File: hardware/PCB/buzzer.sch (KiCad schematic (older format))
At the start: 4 parts

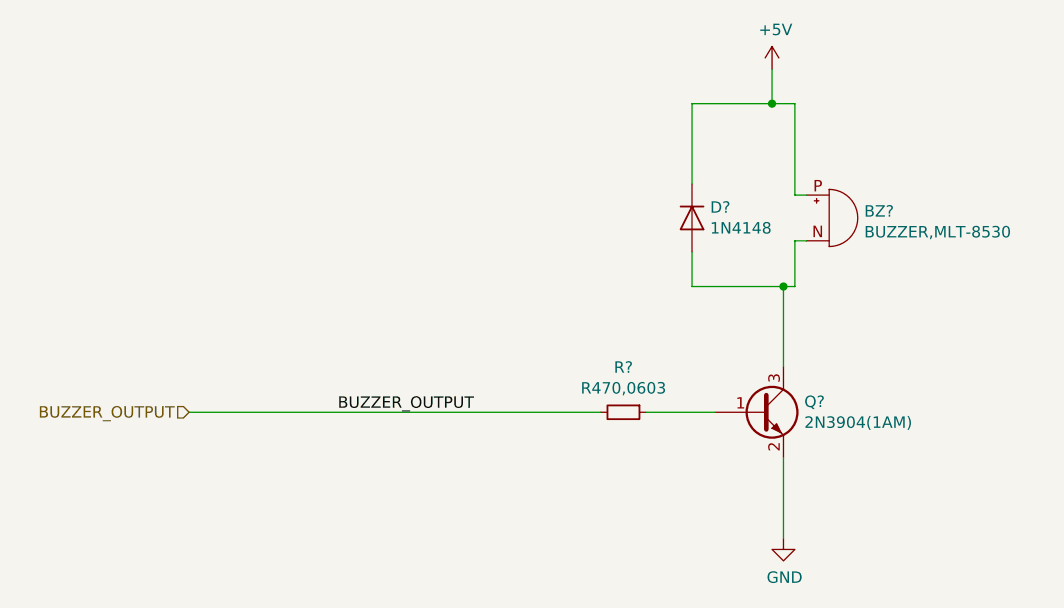
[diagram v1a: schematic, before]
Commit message: sch: update buzzer connection,
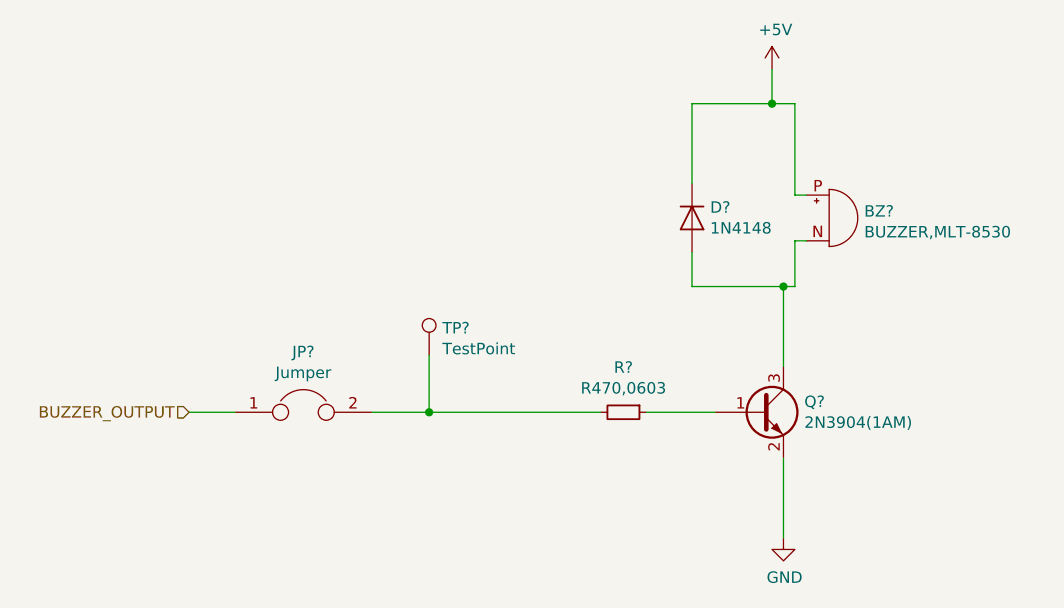
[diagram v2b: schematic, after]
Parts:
- added JP?: Jumper, symbol Device:Jumper
- added TP?: TestPoint, symbol Connector:TestPoint
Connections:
- net BUZZER_OUTPUT: now also JP?.1; no longer R?.2
- new net: JP?.2, R?.2, TP?.1
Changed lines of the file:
@@
 $Descr A4 11693 8268
 encoding utf-8
-Sheet 4 6
+Sheet 1 6
 Title ""
 Date ""
@@
 AR Path="/5E87CEF1/5E91DA5A" Ref="BZ?"  Part="1"
 AR Path="/5E91CDD8/5E91DA5A" Ref="BZ?"  Part="1"
+AR Path="/5E91DA5A" Ref="BZ?"  Part="1"
 F 0 "BZ?" H 8603 2279 50  0000 L CNN
 F 1 "BUZZER,MLT-8530" H 8603 2188 50  0000 L CNN
@@
 AR Path="/5E87CEF1/5E91DA60" Ref="D?"  Part="1"
 AR Path="/5E91CDD8/5E91DA60" Ref="D?"  Part="1"
+AR Path="/5E91DA60" Ref="D?"  Part="1"
 F 0 "D?" V 7804 2329 50  0000 L CNN
 F 1 "1N4148" V 7895 2329 50  0000 L CNN
@@
 AR Path="/5E87CEF1/5E91DA66" Ref="Q?"  Part="1"
 AR Path="/5E91CDD8/5E91DA66" Ref="Q?"  Part="1"
+AR Path="/5E91DA66" Ref="Q?"  Part="1"
 F 0 "Q?" H 8341 3146 50  0000 L CNN
 F 1 "2N3904(1AM)" H 8341 3055 50  0000 L CNN
@@
 AR Path="/5E87CEF1/5E91DA6C" Ref="R?"  Part="1"
 AR Path="/5E91CDD8/5E91DA6C" Ref="R?"  Part="1"
+AR Path="/5E91DA6C" Ref="R?"  Part="1"
 F 0 "R?" V 7354 3100 50  0000 C CNN
 F 1 "R470,0603" V 7445 3100 50  0000 C CNN
@@
 Wire Wire Line
 	8250 3650 8250 3300
-Text Label 6300 3100 0    50   ~ 0
-BUZZER_OUTPUT
-Wire Wire Line
-	5650 3100 7450 3100
 Text HLabel 5650 3100 0    50   Input ~ 0
 BUZZER_OUTPUT
+$Comp
+L Device:Jumper JP?
+U 1 1 5E99CD71
+P 6150 3100
+F 0 "JP?" H 6150 3364 50  0000 C CNN
+F 1 "Jumper" H 6150 3273 50  0000 C CNN
+F 2 "" H 6150 3100 50  0001 C CNN
+F 3 "~" H 6150 3100 50  0001 C CNN
+	1    6150 3100
+	1    0    0    -1
+$EndComp
+Wire Wire Line
+	5850 3100 5650 3100
+Wire Wire Line
+	7450 3100 6700 3100
+$Comp
+L Connector:TestPoint TP?
+U 1 1 5E99F415
+P 6700 2850
+F 0 "TP?" H 6758 2968 50  0000 L CNN
+F 1 "TestPoint" H 6758 2877 50  0000 L CNN
+F 2 "" H 6900 2850 50  0001 C CNN
+F 3 "~" H 6900 2850 50  0001 C CNN
+	1    6700 2850
+	1    0    0    -1
+$EndComp
+Wire Wire Line
+	6700 2850 6700 3100
+Connection ~ 6700 3100
+Wire Wire Line
+	6700 3100 6450 3100
 $EndSCHEMATC

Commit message: update rtl8723 circuit,
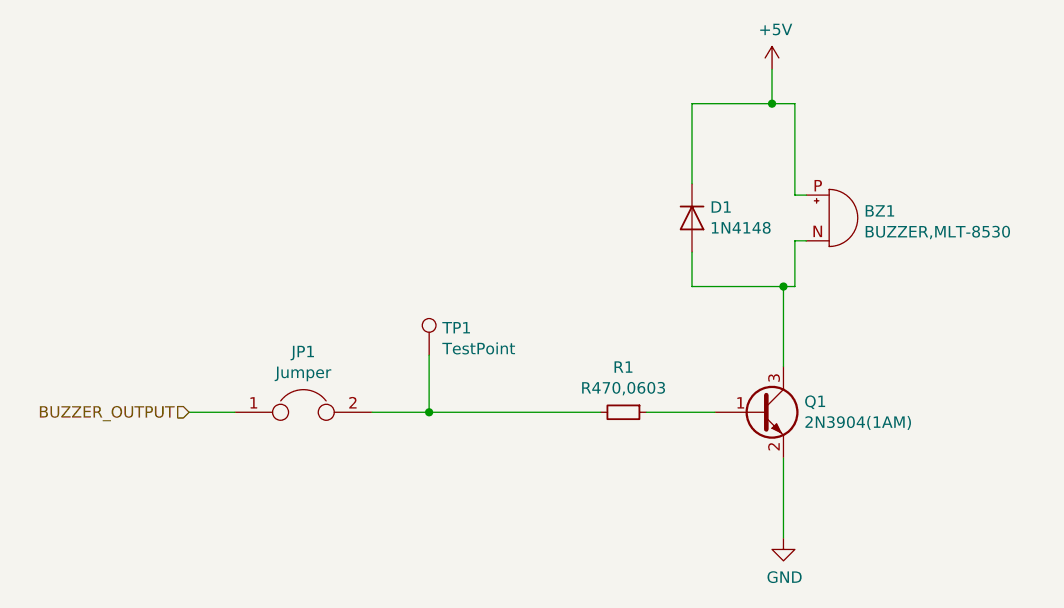
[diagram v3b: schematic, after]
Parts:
- JP1: renamed from JP?; footprint (none) -> Jumper:SolderJumper-2_P1.3mm_Open_TrianglePad1.0x1.5mm
- TP1: renamed from TP?; footprint (none) -> TestPoint:TestPoint_Keystone_5000-5004_Miniature
- gave numbers to parts that had none: 4
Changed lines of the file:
@@
 $Descr A4 11693 8268
 encoding utf-8
-Sheet 1 6
+Sheet 3 6
 Title ""
 Date ""
@@
 P 8450 2250
 AR Path="/5E87CEF1/5E91DA5A" Ref="BZ?"  Part="1"
-AR Path="/5E91CDD8/5E91DA5A" Ref="BZ?"  Part="1"
+AR Path="/5E91CDD8/5E91DA5A" Ref="BZ1"  Part="1"
 AR Path="/5E91DA5A" Ref="BZ?"  Part="1"
-F 0 "BZ?" H 8603 2279 50  0000 L CNN
+F 0 "BZ1" H 8603 2279 50  0000 L CNN
 F 1 "BUZZER,MLT-8530" H 8603 2188 50  0000 L CNN
 F 2 "footprint-lib:MLT-8530" V 8425 2350 50  0001 C CNN
@@
 P 7850 2250
 AR Path="/5E87CEF1/5E91DA60" Ref="D?"  Part="1"
-AR Path="/5E91CDD8/5E91DA60" Ref="D?"  Part="1"
+AR Path="/5E91CDD8/5E91DA60" Ref="D1"  Part="1"
 AR Path="/5E91DA60" Ref="D?"  Part="1"
-F 0 "D?" V 7804 2329 50  0000 L CNN
+F 0 "D1" V 7804 2329 50  0000 L CNN
 F 1 "1N4148" V 7895 2329 50  0000 L CNN
 F 2 "Diode_THT:D_DO-35_SOD27_P7.62mm_Horizontal" H 7850 2075 50  0001 C CNN
@@
 P 8150 3100
 AR Path="/5E87CEF1/5E91DA66" Ref="Q?"  Part="1"
-AR Path="/5E91CDD8/5E91DA66" Ref="Q?"  Part="1"
+AR Path="/5E91CDD8/5E91DA66" Ref="Q1"  Part="1"
 AR Path="/5E91DA66" Ref="Q?"  Part="1"
-F 0 "Q?" H 8341 3146 50  0000 L CNN
+F 0 "Q1" H 8341 3146 50  0000 L CNN
 F 1 "2N3904(1AM)" H 8341 3055 50  0000 L CNN
 F 2 "footprint-lib:MBT3904_1AM_SOT" H 8350 3025 50  0001 L CIN
@@
 P 7550 3100
 AR Path="/5E87CEF1/5E91DA6C" Ref="R?"  Part="1"
-AR Path="/5E91CDD8/5E91DA6C" Ref="R?"  Part="1"
+AR Path="/5E91CDD8/5E91DA6C" Ref="R1"  Part="1"
 AR Path="/5E91DA6C" Ref="R?"  Part="1"
-F 0 "R?" V 7354 3100 50  0000 C CNN
+F 0 "R1" V 7354 3100 50  0000 C CNN
 F 1 "R470,0603" V 7445 3100 50  0000 C CNN
 F 2 "Resistor_SMD:R_0603_1608Metric_Pad1.05x0.95mm_HandSolder" H 7550 3100 50  0001 C CNN
@@
 BUZZER_OUTPUT
 $Comp
-L Device:Jumper JP?
+L Device:Jumper JP1
 U 1 1 5E99CD71
 P 6150 3100
-F 0 "JP?" H 6150 3364 50  0000 C CNN
+F 0 "JP1" H 6150 3364 50  0000 C CNN
 F 1 "Jumper" H 6150 3273 50  0000 C CNN
-F 2 "" H 6150 3100 50  0001 C CNN
+F 2 "Jumper:SolderJumper-2_P1.3mm_Open_TrianglePad1.0x1.5mm" H 6150 3100 50  0001 C CNN
 F 3 "~" H 6150 3100 50  0001 C CNN
 	1    6150 3100
@@
 	7450 3100 6700 3100
 $Comp
-L Connector:TestPoint TP?
+L Connector:TestPoint TP1
 U 1 1 5E99F415
 P 6700 2850
-F 0 "TP?" H 6758 2968 50  0000 L CNN
+F 0 "TP1" H 6758 2968 50  0000 L CNN
 F 1 "TestPoint" H 6758 2877 50  0000 L CNN
-F 2 "" H 6900 2850 50  0001 C CNN
+F 2 "TestPoint:TestPoint_Keystone_5000-5004_Miniature" H 6900 2850 50  0001 C CNN
 F 3 "~" H 6900 2850 50  0001 C CNN
 	1    6700 2850

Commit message: update,
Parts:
- removed D1: 1N4148, Diode_THT:D_DO-35_SOD27_P7.62mm_Horizontal, symbol Diode:1N4148
- added U13: M1,GPP,SMA,DO-214AC,C123825, footprint-lib:DO-214AC, symbol sz_jlc_diode:M1,GPP,SMA,DO-214AC,C123825
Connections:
- net +5V: now also U13.1 (K)
- net at BZ1.N, Q1.3 (C): now also U13.2 (A)
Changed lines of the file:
@@
 $Descr A4 11693 8268
 encoding utf-8
-Sheet 3 6
+Sheet 2 6
 Title ""
 Date ""
@@
 $EndComp
 $Comp
-L Diode:1N4148 D?
-U 1 1 5E91DA60
-P 7850 2250
-AR Path="/5E87CEF1/5E91DA60" Ref="D?"  Part="1"
-AR Path="/5E91CDD8/5E91DA60" Ref="D1"  Part="1"
-AR Path="/5E91DA60" Ref="D?"  Part="1"
-F 0 "D1" V 7804 2329 50  0000 L CNN
-F 1 "1N4148" V 7895 2329 50  0000 L CNN
-F 2 "Diode_THT:D_DO-35_SOD27_P7.62mm_Horizontal" H 7850 2075 50  0001 C CNN
-F 3 "https://assets.nexperia.com/documents/data-sheet/1N4148_1N4448.pdf" H 7850 2250 50  0001 C CNN
-	1    7850 2250
-	0    1    1    0
-$EndComp
-$Comp
 L taobao-transistor:2N3904(1AM) Q?
 U 1 1 5E91DA66
@@
 P 8200 1600
 AR Path="/5E87CEF1/5E91DA72" Ref="#PWR?"  Part="1"
-AR Path="/5E91CDD8/5E91DA72" Ref="#PWR0123"  Part="1"
-F 0 "#PWR0123" H 8200 1450 50  0001 C CNN
+AR Path="/5E91CDD8/5E91DA72" Ref="#PWR09"  Part="1"
+F 0 "#PWR09" H 8200 1450 50  0001 C CNN
 F 1 "+5V" H 8215 1773 50  0000 C CNN
 F 2 "" H 8200 1600 50  0001 C CNN
@@
 	8200 1750 7850 1750
 Wire Wire Line
-	7850 1750 7850 2100
-Wire Wire Line
 	8200 1750 8300 1750
 Wire Wire Line
@@
 Connection ~ 8200 1750
 Wire Wire Line
-	7850 2400 7850 2550
-Wire Wire Line
 	7850 2550 8250 2550
 Wire Wire Line
@@
 P 8250 3650
 AR Path="/5E87CEF1/5E91DA87" Ref="#PWR?"  Part="1"
-AR Path="/5E91CDD8/5E91DA87" Ref="#PWR0124"  Part="1"
-F 0 "#PWR0124" H 8250 3400 50  0001 C CNN
+AR Path="/5E91CDD8/5E91DA87" Ref="#PWR010"  Part="1"
+F 0 "#PWR010" H 8250 3400 50  0001 C CNN
 F 1 "GND" H 8255 3477 50  0000 C CNN
 F 2 "" H 8250 3650 50  0001 C CNN
@@
 Wire Wire Line
 	6700 3100 6450 3100
+$Comp
+L sz_jlc_diode:M1,GPP,SMA,DO-214AC,C123825 U13
+U 1 1 5EA779A4
+P 7850 2250
+F 0 "U13" V 7804 2183 50  0000 R CNN
+F 1 "M1,GPP,SMA,DO-214AC,C123825" V 7895 2183 50  0000 R CNN
+F 2 "footprint-lib:DO-214AC" H 7850 1250 50  0001 C CNN
+F 3 "~" H 7850 2250 50  0001 C CNN
+F 4 "C123825" H 7850 1750 50  0001 C CNN "LCSC_Part"
+F 5 "M1,GPP,SMA,DO-214AC,C123825" H 7900 2050 50  0001 L CNN "MFR_Part"
+F 6 "二极管_通用二极管" H 7850 1650 50  0001 C CNN "Second Category"
+F 7 "SMA,DO-214AC" H 7850 1450 50  0001 C CNN "Package"
+F 8 "2" H 7850 1150 50  0001 C CNN "Solder Joint"
+F 9 "MDD" H 7850 1550 50  0001 C CNN "Manufacturer"
+F 10 "M1 GPP" H 7850 1350 50  0001 C CNN "Library Type"
+	1    7850 2250
+	0    1    1    0
+$EndComp
+Wire Wire Line
+	7850 2350 7850 2550
+Wire Wire Line
+	7850 1750 7850 2150
 $EndSCHEMATC
